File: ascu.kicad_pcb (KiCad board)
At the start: 2 copper layers, 76.9 x 35.9 mm, 91 parts, among them IC1 ATTINY25-SS, P1 B-, P10 CONN_01X01, P11 CONN_01X01, P12 CONN_01X01, P13 CONN_01X01, P14 CONN_01X01, P15 CONN_01X01, P16 CONN_01X01, P17 CONN_01X01, P18 CONN_01X01, P19 CONN_01X01, P2 B+S+, P20 CONN_01X01, P21 CONN_01X01, P22 CONN_01X01, P23 CONN_01X01, P24 CONN_01X01, P25 CONN_01X01, P26 CONN_01X01, P27 CONN_01X01, P28 CONN_01X01, P29 CONN_01X01, P3 S-, P30 CONN_01X01, P31 CONN_01X01, P32 CONN_01X01, P33 CONN_01X01, P34 CONN_01X01, P35 CONN_01X01, P37 Otwór, P38 Otwór, P39 Otwór, P4 CONN_01X01, P40 Otwór, P41 Lut, P42 Lut, P43 Lut, P44 Lut, P45 Lut, P46 Lut, P47 Lut, P48 Lut, P49 Lut, P5 CONN_01X01, P50 Lut, P51 Lut, P52 Lut, P53 Lut, P54 Lut, P55 Lut, P56 Lut, P6 CONN_01X01, P7 CONN_01X01, P8 CONN_01X01, P9 CONN_01X01, Q1 PSMN1R2, Q2 PSMN1R2, SW1 DETECT, SW3 TRIGGER, U1 SPX3819, U2 MIC4605, U3 TLP291

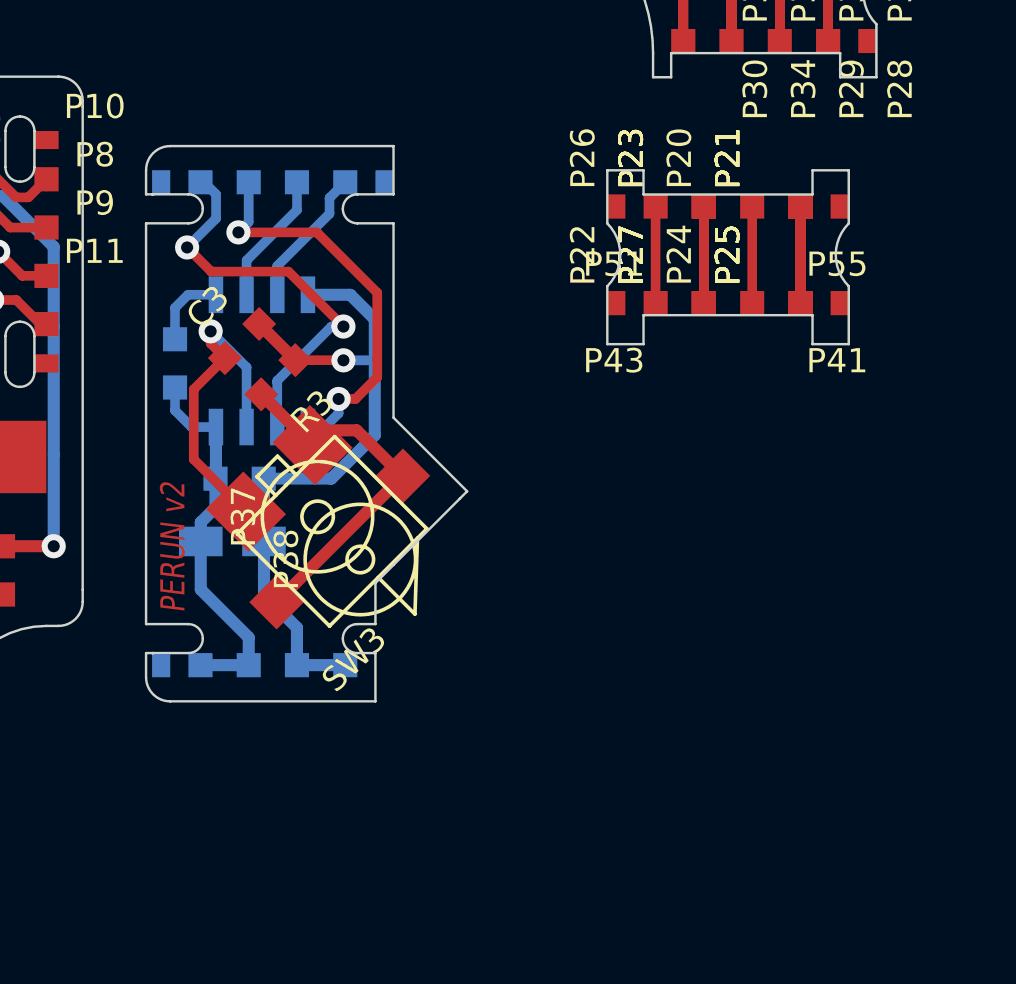
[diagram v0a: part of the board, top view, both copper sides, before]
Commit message: Dodanie szerokiej obudowy
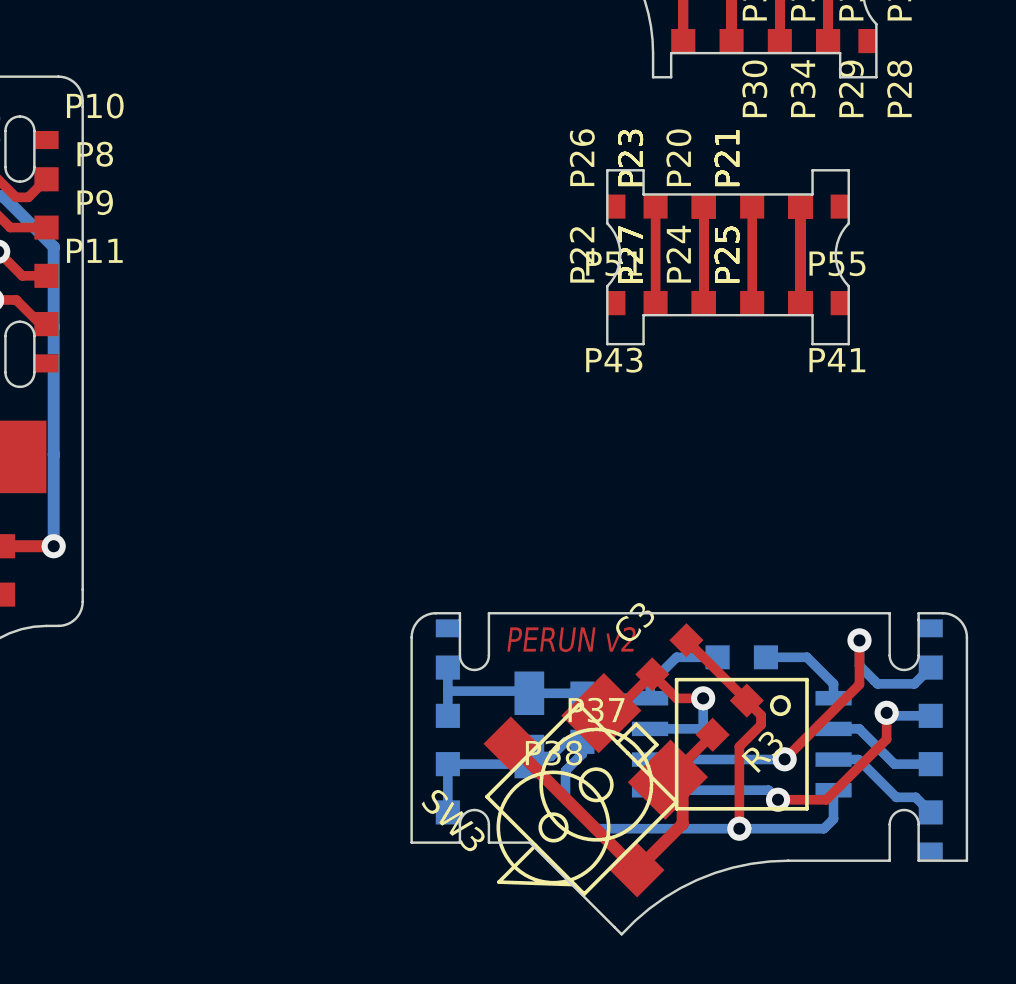
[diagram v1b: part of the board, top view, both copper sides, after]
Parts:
- IC1: footprint 111:SO8 -> 111:WSOIC8
- moved P50 36.8 mm to (188.1, 91.6), turned to 90 degrees
- moved P6 36.3 mm to (188.1, 93.2), turned to 0 degrees
- moved P4 35.9 mm to (188.1, 95.2), turned to 0 degrees
- moved P54 35.8 mm to (188.1, 100.8), turned to 90 degrees
- moved P5 35.6 mm to (188.1, 97.2), turned to 0 degrees
- moved P7 35.6 mm to (188.1, 99.2), turned to 0 degrees
- moved R2 26.4 mm to (180.3, 92.8), turned to 0 degrees
- moved IC1 25.4 mm to (180.3, 96.4), turned to 90 degrees
- moved R3 23.4 mm to (179.8, 95.3)
- moved C3 22.0 mm to (177.3, 92.8)
- moved C4 17.3 mm to (173.7, 95.3), turned to 270 degrees
- moved P37 16.0 mm to (174.3, 98.1), turned to 0 degrees
- moved SW3 14.7 mm to (173.3, 99.0), turned to 135 degrees
- moved C2 14.5 mm to (171.5, 95.6), turned to 270 degrees
- moved P38 13.7 mm to (172.5, 99.8), turned to 0 degrees
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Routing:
- net TRIGGER: track 14.4 -> 9.36 mm
- net G: track 29.0 -> 33.1 mm
- net HIN1: track 16.6 -> 14.0 mm
- net 5: track 15.9 -> 14.3 mm
- net SELECTOR1: track 5.52 -> 4.63 mm
- net DETECT1: track 5.83 -> 4.93 mm
- net RESET: track 3.27 -> 3.85 mm
- net LIN1: track 17.0 -> 16.4 mm
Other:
- board size 76.9 x 35.9 mm -> 80.6 x 42.7 mm
- net class Default: trace_width 0.7 -> 0.4

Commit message: Test
test
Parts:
- moved C2 36.7 mm to (200.5, 73.1)
- moved C3 36.7 mm to (206.3, 70.3)
- moved C4 36.7 mm to (202.7, 72.8)
- moved IC1 36.7 mm to (209.3, 73.9)
- moved P12 36.7 mm to (197.1, 74.7)
- moved P13 36.7 mm to (197.1, 76.7)
- moved P14 36.7 mm to (197.1, 70.7)
- moved P15 36.7 mm to (197.1, 72.7)
- moved P37 36.7 mm to (203.3, 75.6)
- moved P38 36.7 mm to (201.5, 77.3)
- moved P4 36.7 mm to (217.1, 72.7)
- moved P45 36.7 mm to (197.1, 78.3)
- moved P46 36.7 mm to (197.1, 69.1)
- moved P5 36.7 mm to (217.1, 74.7)
- moved P50 36.7 mm to (217.1, 69.1)
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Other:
- board size 80.6 x 42.7 mm -> 109.6 x 35.9 mm

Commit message: Poprawki
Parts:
- moved C2 0.10 mm to (200.5, 73.0)
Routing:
- net LO: track 26.0 -> 26.5 mm
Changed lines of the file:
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@@
     (links 93)
     (no_connects 0)
-    (area 108.899999 58.4 198.783334 110.600001)
+    (area 108.899999 58.4 227.783334 97.550001)
     (thickness 1)
     (drawings 181)
-    (tracks 475)
+    (tracks 478)
     (zones 0)
     (modules 91)
@@
   )
   (module Capacitors_Tantalum_SMD:TantalC_SizeA_EIA-3216_Reflow (layer B.Cu)
-    (at 200.5 73.1 270)
+    (at 200.5 73 270)
     (descr "Tantal Cap. , Size A, EIA-3216, Reflow")
     (tags "Tantal Capacitor Size-A EIA-3216 reflow")
@@
   (gr_line (start 128 81) (end 128 78.5) (angle 90) (layer Margin) (width 0.2))
   (gr_line (start 130 81) (end 128 81) (angle 90) (layer Margin) (width 0.2))
+  (segment (start 131 82.1) (end 131 83) (width 0.6) (layer B.Cu) (net 1))
+  (via (at 131 82.1) (size 1) (drill 0.5) (layers F.Cu B.Cu) (net 1))
+  (segment (start 131.7 83.7) (end 131.7 86.1) (width 0.6) (layer B.Cu) (net 1))
+  (segment (start 131 83) (end 131.7 83.7) (width 0.6) (layer B.Cu) (net 1))
+  (segment (start 131 82.1) (end 131 79.5) (width 0.5) (layer F.Cu) (net 1))
+  (segment (start 123 82.8) (end 123.7 82.1) (width 0.5) (layer F.Cu) (net 1))
+  (segment (start 123.7 82.1) (end 131 82.1) (width 0.5) (layer F.Cu) (net 1))
+  (segment (start 121.9 82.8) (end 123 82.8) (width 0.5) (layer F.Cu) (net 1) (status 400000))
+  (segment (start 131 79.5) (end 131.5 79) (width 0.5) (layer F.Cu) (net 1) (status 800000))
   (segment (start 120.3 85.1) (end 121.1 85.1) (width 0.5) (layer F.Cu) (net 1))
+  (segment (start 121.1 85.1) (end 121.9 84.3) (width 0.5) (layer F.Cu) (net 1))
   (segment (start 121.9 84.3) (end 121.9 82.8) (width 0.5) (layer F.Cu) (net 1))
-  (segment (start 121.1 85.1) (end 121.9 84.3) (width 0.5) (layer F.Cu) (net 1))
-  (segment (start 121.9 82.8) (end 125.8 82.8) (width 0.5) (layer F.Cu) (net 1))
-  (segment (start 131.4 82.1) (end 131.5 82.2) (width 0.5) (layer F.Cu) (net 1))
-  (segment (start 126.5 82.1) (end 131.4 82.1) (width 0.5) (layer F.Cu) (net 1))
-  (segment (start 125.8 82.8) (end 126.5 82.1) (width 0.5) (layer F.Cu) (net 1))
   (segment (start 135.15 90.4) (end 135.15 91.8) (width 0.6) (layer B.Cu) (net 1))
   (segment (start 135.15 91.8) (end 134.9 91.8) (width 0.6) (layer B.Cu) (net 1))
@@
   (segment (start 131.7 86.1) (end 131.9 86.1) (width 0.6) (layer B.Cu) (net 1))
   (segment (start 131.9 86.1) (end 131.7 86.1) (width 0.6) (layer B.Cu) (net 1))
-  (segment (start 131.5 82.2) (end 131.5 82.25) (width 0.6) (layer F.Cu) (net 1))
-  (segment (start 131.5 79) (end 131.5 82.25) (width 0.5) (layer F.Cu) (net 1))
-  (via (at 131.5 82.2) (size 1) (drill 0.5) (layers F.Cu B.Cu) (net 1))
-  (segment (start 131.7 86.1) (end 131.7 82.4) (width 0.6) (layer B.Cu) (net 1))
-  (segment (start 131.7 82.4) (end 131.5 82.2) (width 0.6) (layer B.Cu) (net 1))
   (segment (start 131.7 91.3) (end 131.7 86.1) (width 0.6) (layer B.Cu) (net 1))
+  (segment (start 132.2 91.8) (end 131.7 91.3) (width 0.6) (layer B.Cu) (net 1))
   (segment (start 134.9 91.8) (end 132.2 91.8) (width 0.6) (layer B.Cu) (net 1))
-  (segment (start 132.2 91.8) (end 131.7 91.3) (width 0.6) (layer B.Cu) (net 1))
   (segment (start 142.375 94) (end 143 94) (width 1.2) (layer F.Cu) (net 1))
   (segment (start 143 94) (end 144.5 92.5) (width 1.2) (layer F.Cu) (net 1))
@@
   (segment (start 203.656371 72.635913) (end 203.664087 72.635913) (width 0.4) (layer F.Cu) (net 11))
   (segment (start 205.5 71.995) (end 202.895 71.995) (width 0.4) (layer B.Cu) (net 12))
-  (segment (start 202.895 71.995) (end 202.7 71.8) (width 0.4) (layer B.Cu) (net 12))
   (segment (start 200.5 71.79) (end 202.69 71.79) (width 0.4) (layer B.Cu) (net 12))
-  (segment (start 202.69 71.79) (end 202.7 71.8) (width 0.4) (layer B.Cu) (net 12))
   (segment (start 197.125 71.7) (end 200.41 71.7) (width 0.4) (layer B.Cu) (net 12))
   (segment (start 200.41 71.7) (end 200.5 71.79) (width 0.4) (layer B.Cu) (net 12))
+  (segment (start 202.895 71.995) (end 202.7 71.8) (width 0.4) (layer B.Cu) (net 12))
+  (segment (start 202.69 71.79) (end 202.7 71.8) (width 0.4) (layer B.Cu) (net 12))
   (segment (start 197.125 72.725) (end 197.125 71.7) (width 0.4) (layer B.Cu) (net 12))
   (segment (start 197.125 71.7) (end 197.125 70.725) (width 0.4) (layer B.Cu) (net 12))
@@
   (segment (start 205.5 71.4) (end 205.5 71.995) (width 0.4) (layer B.Cu) (net 12))
   (segment (start 206.6 70.3) (end 205.5 71.4) (width 0.4) (layer B.Cu) (net 12))
-  (segment (start 209.507107 72.092893) (end 209.507107 72.107107) (width 0.4) (layer F.Cu) (net 13))
-  (segment (start 209.507107 72.107107) (end 210.1 72.7) (width 0.4) (layer F.Cu) (net 13))
-  (via (at 209.2 77.4) (size 1) (drill 0.5) (layers F.Cu B.Cu) (net 13))
-  (segment (start 209.2 74) (end 209.2 77.4) (width 0.4) (layer F.Cu) (net 13))
-  (segment (start 210.1 73.1) (end 209.2 74) (width 0.4) (layer F.Cu) (net 13))
-  (segment (start 210.1 72.7) (end 210.1 73.1) (width 0.4) (layer F.Cu) (net 13))
+  (segment (start 209.507107 72.092893) (end 209.507107 72.107107) (width 0.4) (layer F.Cu) (net 13) (status C00000))
+  (segment (start 209.507107 72.107107) (end 210.2 72.8) (width 0.4) (layer F.Cu) (net 13) (status 400000))
+  (segment (start 209.1 77.4) (end 209.2 77.4) (width 0.4) (layer B.Cu) (net 13))
+  (via (at 209.1 77.4) (size 1) (drill 0.5) (layers F.Cu B.Cu) (net 13))
+  (segment (start 209.1 74.7) (end 209.1 77.4) (width 0.4) (layer F.Cu) (net 13))
+  (segment (start 210.2 73.6) (end 209.1 74.7) (width 0.4) (layer F.Cu) (net 13))
+  (segment (start 210.2 72.8) (end 210.2 73.6) (width 0.4) (layer F.Cu) (net 13))
+  (segment (start 200.5 74.41) (end 201.39 74.41) (width 0.4) (layer B.Cu) (net 13))
+  (segment (start 201.39 74.41) (end 202 73.8) (width 0.4) (layer B.Cu) (net 13))
+  (segment (start 202 73.8) (end 202.7 73.8) (width 0.4) (layer B.Cu) (net 13))
+  (segment (start 197.125 74.725) (end 200.185 74.725) (width 0.4) (layer B.Cu) (net 13))
+  (segment (start 202.7 74.3) (end 202 75) (width 0.4) (layer B.Cu) (net 13))
+  (segment (start 202 75) (end 202 76.2) (width 0.4) (layer B.Cu) (net 13))
+  (segment (start 202 76.2) (end 203.2 77.4) (width 0.4) (layer B.Cu) (net 13))
+  (segment (start 203.2 77.4) (end 209.2 77.4) (width 0.4) (layer B.Cu) (net 13))
+  (segment (start 202.7 73.8) (end 202.7 74.3) (width 0.4) (layer B.Cu) (net 13))
+  (segment (start 200.185 74.725) (end 200.5 74.41) (width 0.4) (layer B.Cu) (net 13))
   (segment (start 209.507107 72.092893) (end 207.007107 69.592893) (width 0.4) (layer F.Cu) (net 13))
-  (segment (start 202.7 73.8) (end 202.7 74.3) (width 0.4) (layer B.Cu) (net 13))
-  (segment (start 202.7 74.3) (end 202 75) (width 0.4) (layer B.Cu) (net 13))
   (segment (start 213.1 77) (end 213.1 75.805) (width 0.4) (layer B.Cu) (net 13))
   (segment (start 212.7 77.4) (end 213.1 77) (width 0.4) (layer B.Cu) (net 13))
-  (segment (start 203.2 77.4) (end 209.2 77.4) (width 0.4) (layer B.Cu) (net 13))
   (segment (start 209.2 77.4) (end 212.7 77.4) (width 0.4) (layer B.Cu) (net 13))
-  (segment (start 202 76.2) (end 203.2 77.4) (width 0.4) (layer B.Cu) (net 13))
-  (segment (start 202 75) (end 202 76.2) (width 0.4) (layer B.Cu) (net 13))
-  (segment (start 200.5 74.41) (end 201.39 74.41) (width 0.4) (layer B.Cu) (net 13))
-  (segment (start 202 73.8) (end 202.7 73.8) (width 0.4) (layer B.Cu) (net 13))
-  (segment (start 201.39 74.41) (end 202 73.8) (width 0.4) (layer B.Cu) (net 13))
-  (segment (start 197.125 74.725) (end 200.185 74.725) (width 0.4) (layer B.Cu) (net 13))
-  (segment (start 200.185 74.725) (end 200.5 74.41) (width 0.4) (layer B.Cu) (net 13))
   (segment (start 197.125 76.725) (end 197.125 74.725) (width 0.4) (layer B.Cu) (net 13))
   (segment (start 213.1 73.265) (end 214.165 73.265) (width 0.4) (layer B.Cu) (net 14))
@@
   (segment (start 146.5 77.4) (end 146.5 80.2) (width 0.4) (layer F.Cu) (net 29))
   (segment (start 146.635 77.265) (end 146.5 77.4) (width 0.4) (layer F.Cu) (net 29))
-  (segment (start 149.7 88.2) (end 151.8 88.2) (width 0.5) (layer F.Cu) (net 30))
-  (segment (start 144.095 72.305) (end 144.095 70.76) (width 0.5) (layer F.Cu) (net 30))
-  (segment (start 143.7 72.7) (end 144.095 72.305) (width 0.5) (layer F.Cu) (net 30))
-  (via (at 143.7 72.7) (size 1) (drill 0.5) (layers F.Cu B.Cu) (net 30))
-  (segment (start 144.7 73.7) (end 143.7 72.7) (width 0.5) (layer B.Cu) (net 30))
-  (segment (start 149.7 73.7) (end 144.7 73.7) (width 0.5) (layer B.Cu) (net 30))
-  (segment (start 151.8 75.8) (end 149.7 73.7) (width 0.5) (layer B.Cu) (net 30))
-  (segment (start 151.8 79.1) (end 151.8 75.8) (width 0.5) (layer B.Cu) (net 30))
-  (segment (start 151.8 84.4) (end 151.8 79.1) (width 0.5) (layer B.Cu) (net 30))
-  (segment (start 151.8 88.2) (end 151.8 84.4) (width 0.5) (layer B.Cu) (net 30))
+  (segment (start 149.7 88.2) (end 151.8 88.2) (width 0.4) (layer F.Cu) (net 30) (status 400000))
+  (segment (start 144.095 72.205) (end 144.095 70.76) (width 0.4) (layer F.Cu) (net 30) (status 800000))
+  (segment (start 143.8 72.5) (end 144.095 72.205) (width 0.4) (layer F.Cu) (net 30))
+  (via (at 143.8 72.5) (size 1) (drill 0.5) (layers F.Cu B.Cu) (net 30))
+  (segment (start 143.8 73.3) (end 143.8 72.5) (width 0.4) (layer B.Cu) (net 30))
+  (segment (start 144.8 74.3) (end 143.8 73.3) (width 0.4) (layer B.Cu) (net 30))
+  (segment (start 150.8 74.3) (end 144.8 74.3) (width 0.4) (layer B.Cu) (net 30))
+  (segment (start 151.8 75.3) (end 150.8 74.3) (width 0.4) (layer B.Cu) (net 30))
+  (segment (start 151.8 77.6) (end 151.8 75.3) (width 0.4) (layer B.Cu) (net 30))
+  (segment (start 151.8 81.7) (end 151.8 77.6) (width 0.4) (layer B.Cu) (net 30))
+  (segment (start 151.8 86.1) (end 151.8 81.7) (width 0.4) (layer B.Cu) (net 30))
+  (segment (start 151.8 88.2) (end 151.8 86.1) (width 0.4) (layer B.Cu) (net 30))
   (via (at 151.8 88.2) (size 1) (drill 0.5) (layers F.Cu B.Cu) (net 30))
   (zone (net 0) (net_name "") (layer B.Paste) (hatch none 0.508)
